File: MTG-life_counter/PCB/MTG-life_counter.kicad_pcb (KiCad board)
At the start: 2 copper layers, 65 x 43 mm, 45 parts, among them J1 USB_B_Mini, J2 AVR-ISP-6, Q1 IRLML6244, Q2 Si2301DS, Q3 Si2301DS, U1 MCP73831-2-OT, U2 AT90S4433-8P, U3 HDSP-H101, U4 HDSP-H101, U5 SGM809-T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

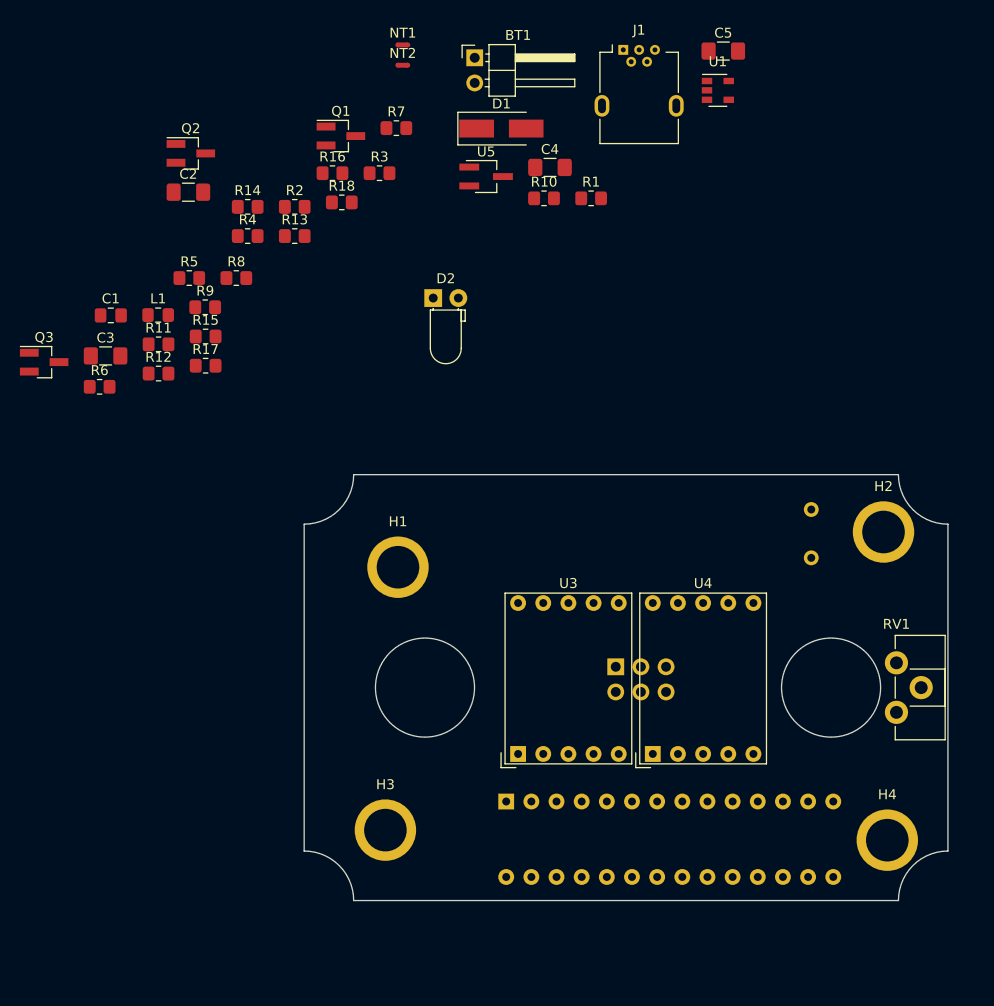
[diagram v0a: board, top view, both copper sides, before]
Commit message: Placement of (mounting) holes, 7-seg. displays and programming socket.
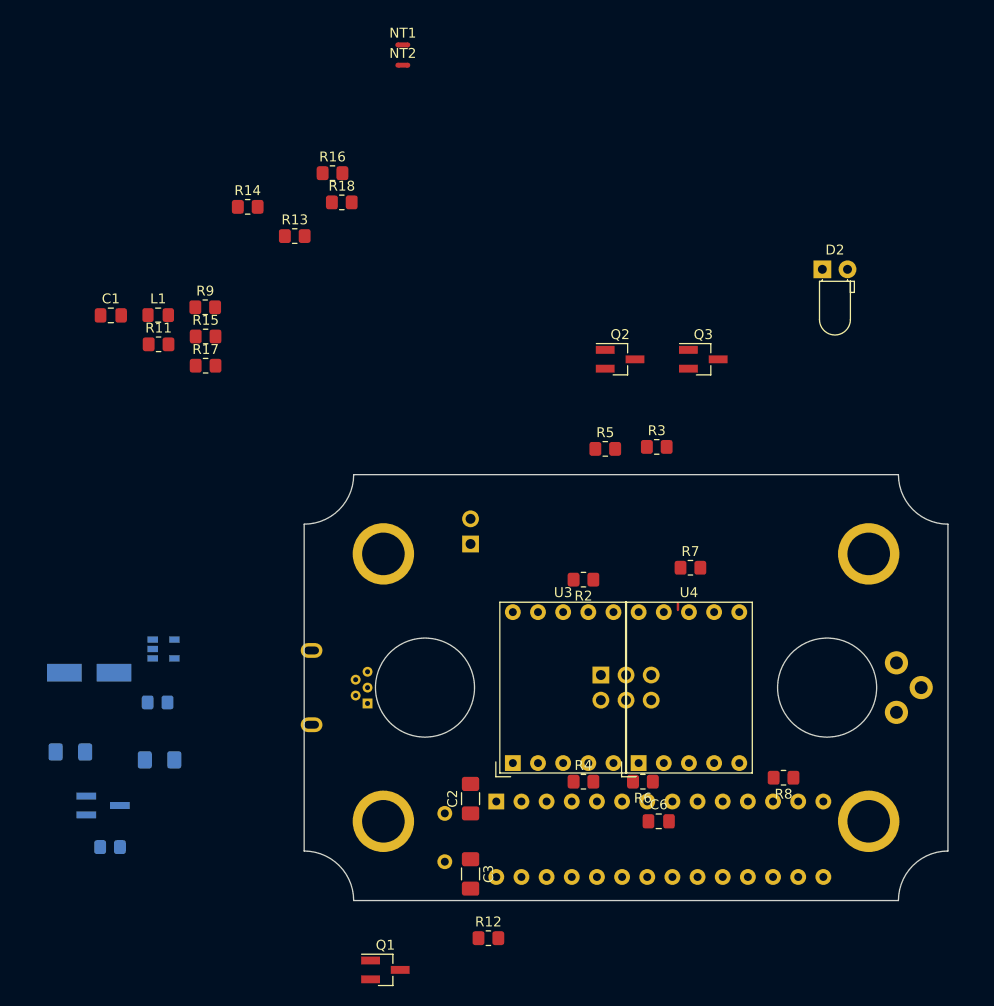
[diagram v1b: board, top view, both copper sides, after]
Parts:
- added C6: 100 nF, Capacitor_SMD:C_0805_2012Metric_Pad1.18x1.45mm_HandSolder, F.Cu at (135.8, 135.0)
- BT1, C4, C5, D1, H1, H2, H3, H4, J1, R1, R10, RV1, U1, U5: moved to B.Cu
- moved C5 91.4 mm to (85.4, 128.8)
- moved Q1 84.3 mm to (108.2, 150.0)
- moved U1 79.5 mm to (85.8, 117.6)
- moved R10 78.8 mm to (80.4, 137.6)
- moved C4 76.3 mm to (76.4, 128.0)
- moved R8 74.8 mm to (148.4, 130.6), turned to 180 degrees
- moved U5 74.3 mm to (79.7, 133.4)
- moved J1 70.9 mm to (106.4, 123.1), turned to 90 degrees
- moved D1 68.9 mm to (78.3, 120.0)
- moved R6 67.8 mm to (134.2, 131.0), turned to 180 degrees
- moved C2 67.5 mm to (116.8, 132.7), turned to 90 degrees
- moved R1 67.1 mm to (85.2, 123.0)
- moved Q3 66.5 mm to (140.3, 88.3)
- moved R12 66.0 mm to (118.6, 146.8)
- moved R4 64.7 mm to (128.2, 131.0)
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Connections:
- net Net-(C2-Pad1) renamed /XTAL1
- net Net-(C3-Pad1) renamed /XTAL2
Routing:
- net /7S_F: track 0.00 -> 0.70 mm
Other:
- outline, holes or cut-outs redrawn

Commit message: The placing & routing is pretty much done, except GND.
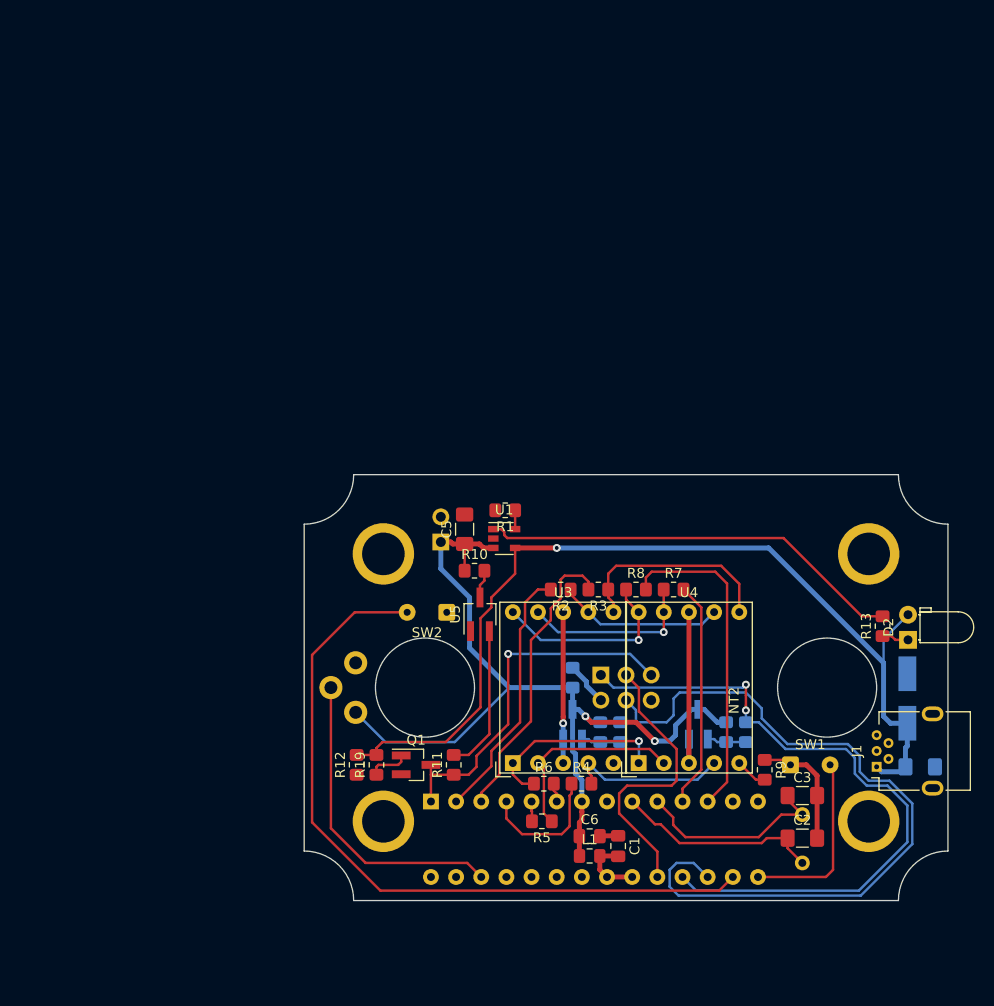
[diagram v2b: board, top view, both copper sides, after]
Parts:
- added R19: 10 kΩ, Resistor_SMD:R_0805_2012Metric_Pad1.20x1.40mm_HandSolder, F.Cu at (107.3, 129.3)
- added SW1: SW_Push, Connector_Wire:SolderWire-0.15sqmm_1x02_P4mm_D0.5mm_OD1.5mm, F.Cu at (149.1, 129.3)
- added SW2: SW_Push, Connector_Wire:SolderWire-0.15sqmm_1x02_P4mm_D0.5mm_OD1.5mm, F.Cu at (114.4, 113.9)
- C5, J1, R1, R10, U1, U5: moved to F.Cu
- NT1: footprint NetTie:NetTie-2_SMD_Pad0.5mm -> mibe:NetTie-2_SMD_Pad0.25mm; moved to B.Cu
- NT2: footprint NetTie:NetTie-2_SMD_Pad0.5mm -> mibe:NetTie-2_SMD_Pad0.25mm
- Q2, Q3, R14, R15, R16, R17, R18: moved to B.Cu
- moved C4 85.8 mm to (162.2, 129.5)
- moved D1 82.6 mm to (160.9, 122.6), turned to 90 degrees
- moved C1 74.1 mm to (131.7, 137.5), turned to 270 degrees
- moved R9 73.3 mm to (146.5, 129.8), turned to 270 degrees
- moved NT2 72.9 mm to (144.6, 122.8), turned to 90 degrees
- moved NT1 71.9 mm to (133.5, 124.5), turned to 270 degrees
- moved R13 71.2 mm to (158.4, 115.3), turned to 90 degrees
- moved L1 69.9 mm to (128.8, 138.5)
- moved R15 67.6 mm to (144.6, 126.0), turned to 270 degrees
- moved R18 66.1 mm to (142.6, 126.0), turned to 270 degrees
- moved R14 65.0 mm to (131.9, 126.0), turned to 90 degrees
- moved R16 56.4 mm to (127.1, 120.5), turned to 90 degrees
- moved RV1 54.8 mm to (105.2, 119.0), turned to 180 degrees
- moved R17 54.4 mm to (129.9, 126.0), turned to 270 degrees
- moved R11 51.9 mm to (115.1, 129.3), turned to 90 degrees
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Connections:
- net Net-(J2-Pad2) renamed /VCC_PROG
- net Net-(Q2-Pad2) renamed /CA_1
- net Net-(Q3-Pad2) renamed /CA_2
- net Net-(RV1-Pad2) renamed /BRIGHTNESS
- Q1 pad 1: /Power/VUSB -> Net-(Q1-Pad1)
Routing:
- net /Power/VUSB: track 0.00 -> 96.2 mm, vias 0 -> 1
- net +BATT: track 0.00 -> 90.5 mm, vias 0 -> 2
- net /~DIGIT_1_ENABLE: track 0.00 -> 75.4 mm
- net /SW_INC: track 0.00 -> 74.2 mm
- net /~DIGIT_2_ENABLE: track 0.00 -> 51.4 mm, vias 0 -> 1
- net /Power/CHARGER_STAT: track 0.00 -> 43.1 mm
- net ~RESET: track 0.00 -> 36.7 mm, vias 0 -> 1
- net Net-(R8-Pad2): track 0.00 -> 33.0 mm
- net /BRIGHTNESS: track 0.00 -> 31.4 mm
- net Net-(R3-Pad2): track 0.00 -> 29.7 mm
- net SCK: track 0.00 -> 29.1 mm
- net Net-(R2-Pad2): track 0.00 -> 26.1 mm
- net Net-(R7-Pad2): track 0.00 -> 23.1 mm
- net /7S_B: track 0.00 -> 21.3 mm
- net /XTAL1: track 0.00 -> 20.8 mm
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
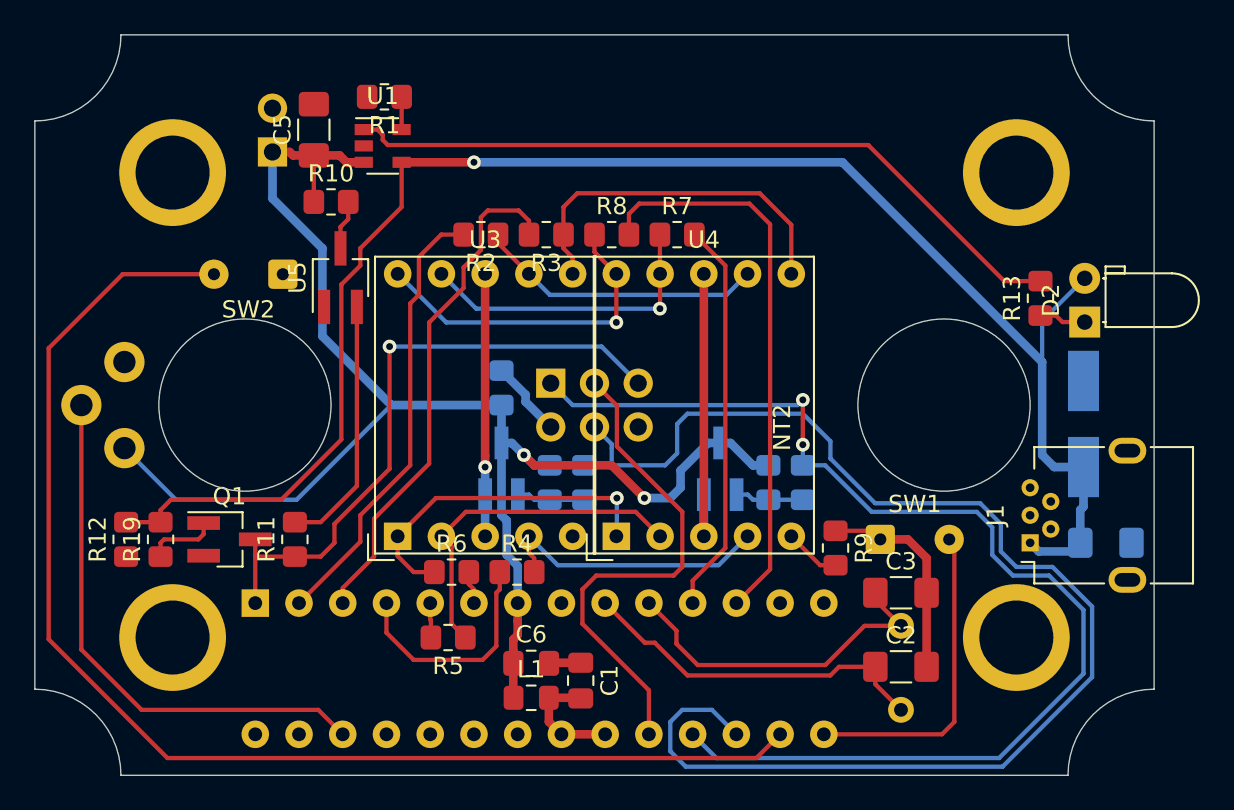
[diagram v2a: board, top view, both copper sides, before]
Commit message: All references are moved to a visible location.
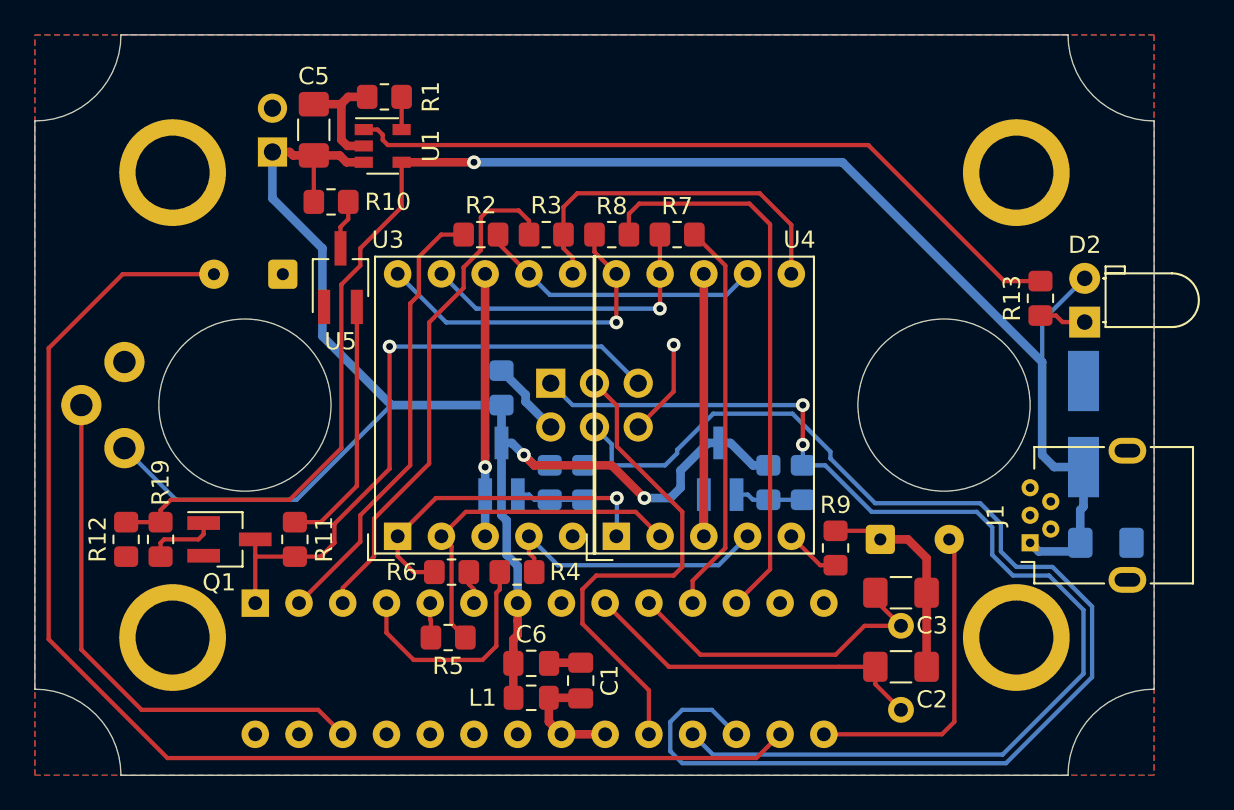
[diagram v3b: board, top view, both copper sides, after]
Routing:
- net GND: track 14.4 -> 26.8 mm, vias 0 -> 1
- net /~DIGIT_1_ENABLE: track 75.4 -> 74.0 mm
- net /XTAL2: track 20.1 -> 19.1 mm
- added copper zone on B.Cu, net GND
- added copper zone on F.Cu, net GND

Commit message: Add text to silkscreen.
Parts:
- added REF**: OSHW-Logo_5.7x6mm_SilkScreen, Symbol:OSHW-Logo_5.7x6mm_SilkScreen, F.Cu at (150.5, 111.0)
- added REF**: Symbol_Attention_SilkTop_Small, mibe:Symbol_Attention_SilkTop_Small, B.Cu at (134.3, 106.1)
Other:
- board text added: "+"
- board text added: "-"
- board text added: "Bottom"
- board text added: "Disconnect the battery before connecting a programmer!"
- board text added: "MTG life counter http://michis-pla.net"
- board text added: "OHL 1.2"
- board text added: "Observe battery polarity!"
- board text added: "Rev. 22/1"
- board text added: "Top"

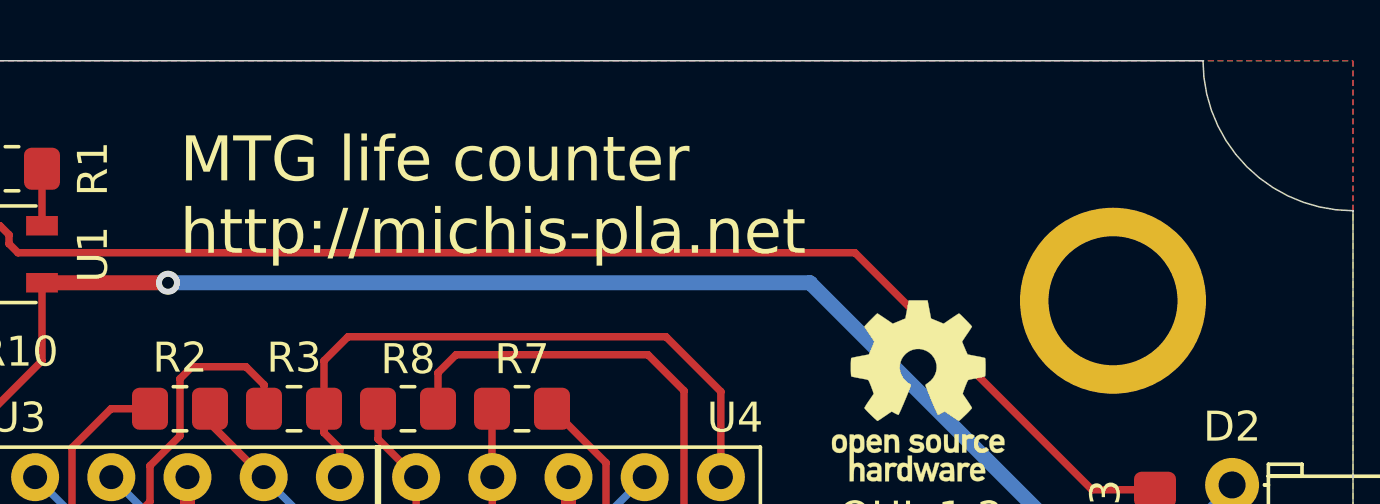
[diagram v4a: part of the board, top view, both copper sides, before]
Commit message: Improved the silkscreen a bit.
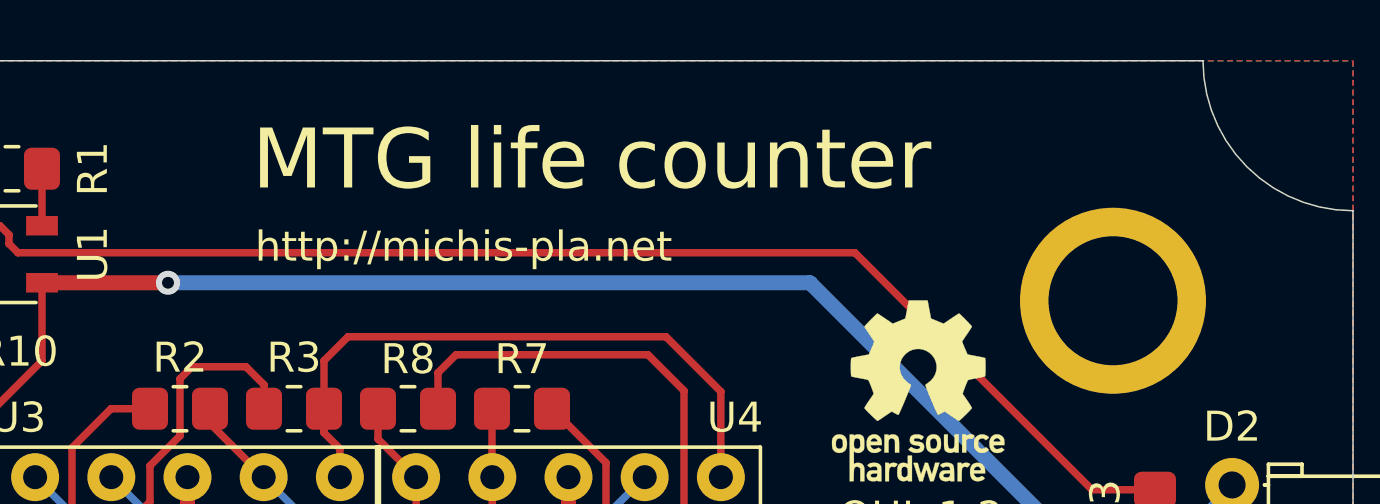
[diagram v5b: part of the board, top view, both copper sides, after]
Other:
- board text added: "MTG life counter"
- board text added: "http://michis-pla.net"
- board text removed: "MTG life counter http://michis-pla.net"

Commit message: Removed brightness feature.
This closes #11.
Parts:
- removed RV1: 10 kΩ, Potentiometer_THT:Potentiometer_Piher_PT-10-H01_Horizontal
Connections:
- U2 pad 26: /BRIGHTNESS -> Net-(U2-Pad26)
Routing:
- net /BRIGHTNESS: track 31.4 -> 0.00 mm

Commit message: Remove R16 to fix #8.
The chances of the battery and programmer connected at the same time is there but actually pretty low. To flash the micro-controller you would disconnect the battery because of the easier handling alone...
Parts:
- removed R16: 150 Ω, Resistor_SMD:R_0805_2012Metric_Pad1.20x1.40mm_HandSolder
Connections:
- J2 pad 2: /VCC_PROG -> +BATT
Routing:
- net /VCC_PROG: track 4.45 -> 0.00 mm
- net +BATT: track 90.5 -> 92.3 mm

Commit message: Change the USB B mini charging connector to USB C (see #6). Still needs to be placed and routed.
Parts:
- added R16: 5,1 kΩ, Resistor_SMD:R_0805_2012Metric_Pad1.20x1.40mm_HandSolder, F.Cu at (154.4, 85.5)
- added R20: 5,1 kΩ, Resistor_SMD:R_0805_2012Metric_Pad1.20x1.40mm_HandSolder, F.Cu at (154.4, 88.4)
- J1: value USB_B_Mini -> USB_C_Receptacle; footprint mibe:USB_Mini-B_Reichelt_BWM -> mibe:USB_C_Receptacle_Bellwether_80211-x92
- moved J1 35.7 mm to (144.8, 96.2), turned to 180 degrees
